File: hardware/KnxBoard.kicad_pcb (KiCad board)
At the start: 4 copper layers, 43 parts, among them J1 Conn_01x16, J2 Conn_01x16, J3 Conn_01x12, J4 Conn_01x02_Male, U0 STM32U575CIT6, U1 NCN5130, X1 FA-238

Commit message: Progress
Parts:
- C14, C19, C5_9, C6, JP0, JP1, R3: moved to B.Cu
- C16, C17: moved to F.Cu
- moved C12 47.0 mm to (113.3, 55.4), turned to 90 degrees
- moved R1 46.6 mm to (103.1, 53.3), turned to 180 degrees
- moved C16 44.5 mm to (98.6, 57.9), turned to 0 degrees
- moved C6 40.8 mm to (109.2, 57.4), turned to -90 degrees
- moved C14 37.9 mm to (102.1, 54.4), turned to 180 degrees
- moved R3 37.4 mm to (104.1, 65.0), turned to 180 degrees
- moved C17 37.4 mm to (95.5, 54.4), turned to 90 degrees
- moved C13 35.1 mm to (100.6, 62.5), turned to -90 degrees
- moved C10 33.5 mm to (98.6, 59.9)
- moved C20 32.1 mm to (115.8, 62.0), turned to 90 degrees
- moved R5 32.0 mm to (110.2, 65.0)
- moved R2 29.3 mm to (94.5, 67.1), turned to 180 degrees
- moved C15 28.8 mm to (113.3, 62.0), turned to -90 degrees
- moved R4 24.6 mm to (104.1, 65.0)
- moved C19 23.8 mm to (93.0, 71.1), turned to 90 degrees
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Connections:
- C6 pad 2: GND -> GNDREF
- JP2 pad 2: /MCU/PH1 -> KNX_RESETB
- U1 pad 23: GND -> GNDREF
- U1 pad 24: GND -> GNDREF
- U1 pad 25: GND -> GNDREF
- U1 pad 26: GND -> GNDREF
- U1 pad 29: GND -> GNDREF
- U1 pad 31: GND -> GNDREF
- U1 pad 33: GND -> GNDREF
- U1 pad 41: GND -> GNDREF
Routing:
- net GNDREF: track 100.1 -> 232.5 mm, vias 5 -> 13
- net KNX_RESETB: track 0.00 -> 72.0 mm, vias 0 -> 1
- net KNX_RXD: track 1.60 -> 62.7 mm, vias 1 -> 3
- net KNX_TXD: track 0.00 -> 55.9 mm, vias 0 -> 3
- net VDD: track 115.2 -> 166.7 mm, vias 7 -> 6
- net +3V3: track 0.00 -> 43.5 mm, vias 0 -> 3
- net Net-(C14-Pad2): track 0.00 -> 40.4 mm, vias 0 -> 2
- net KNX_SAVEB: track 0.00 -> 39.2 mm, vias 0 -> 2
- net +12V: track 0.00 -> 29.6 mm, vias 0 -> 1
- net Net-(R6-Pad1): track 0.00 -> 26.8 mm, vias 0 -> 2
- net /KNXIFACE/Vfilt: track 0.00 -> 23.9 mm, vias 0 -> 3
- net Net-(C17-Pad2): track 0.00 -> 20.6 mm, vias 0 -> 2
- net Led: track 32.8 -> 16.5 mm
- net Net-(L1-Pad1): track 0.00 -> 15.8 mm, vias 0 -> 2
- net /MCU/DEBUG_JTMS-SWDIO: track 27.3 -> 11.9 mm, vias 1 -> 0
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- added copper zone on B.Cu, net GNDREF
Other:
- board outline added: 41.8 x 41.9 mm

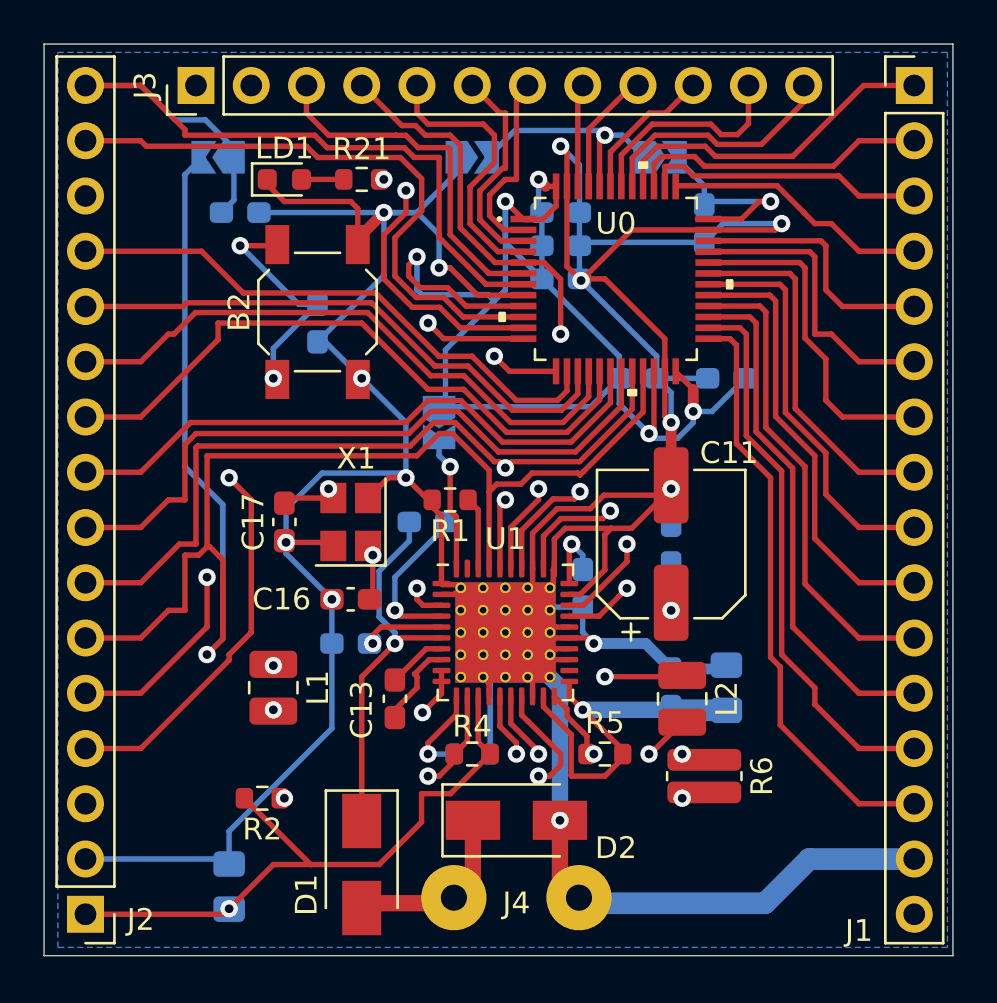
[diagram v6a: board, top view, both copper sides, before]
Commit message: Switch to STM32G491KEU6 with NCN5130
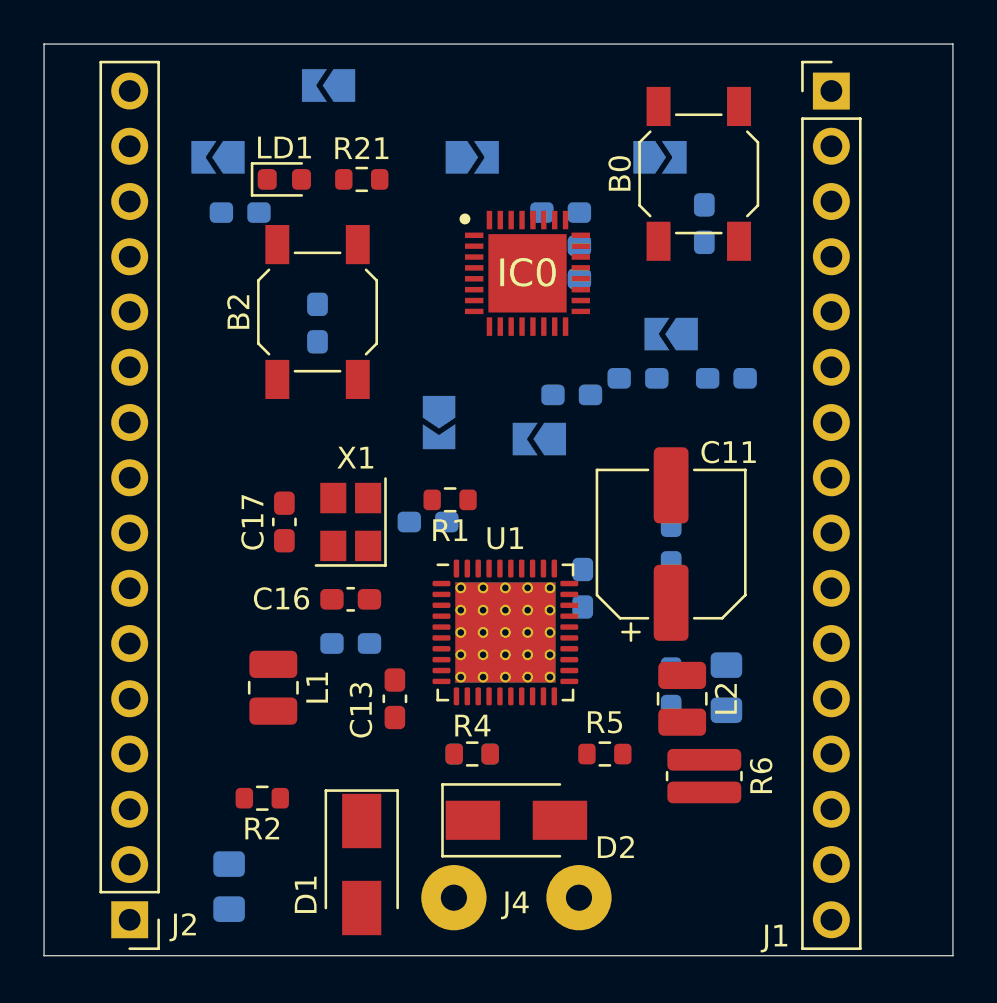
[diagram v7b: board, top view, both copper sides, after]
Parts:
- removed J3: Conn_01x12, Connector_PinHeader_2.54mm:PinHeader_1x12_P2.54mm_Vertical
- removed U0: STM32U575CIT6, KnxBoard:STM32U575CIT6
- added B0: RESET, Button_Switch_SMD:SW_SPST_SKQG_WithStem, F.Cu at (114.6, 38.4)
- added C1: 100 nF, Capacitor_SMD:C_0603_1608Metric_Pad1.08x0.95mm_HandSolder, B.Cu at (108.7, 48.5)
- added IC0: STM32G491KEU6, KnxBoard:STM32G491KEU6, F.Cu at (106.7, 42.9)
- added JP4: Bootflash, Jumper:SolderJumper-2_P1.3mm_Open_TrianglePad1.0x1.5mm, B.Cu at (97.5, 34.3)
- added JP5: Bootloader, Jumper:SolderJumper-2_P1.3mm_Open_TrianglePad1.0x1.5mm, B.Cu at (113.3, 45.7)
- added JP6: RESETB_NRST, Jumper:SolderJumper-2_P1.3mm_Open_TrianglePad1.0x1.5mm, B.Cu at (107.2, 50.5)
- moved J1 3.82 mm to (120.7, 34.5)
- moved J2 2.05 mm to (88.4, 72.6)
- renumbered C3_48 to C3, C3_36 to C4, C3_25 to C5
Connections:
- C5 pad 1: VDD -> GNDREF
- C5 pad 2: GNDREF -> VDD
- J1 pad 1: /MCU/PB4 -> GNDREF
- J1 pad 10: /MCU/PA8 -> /MCU/DEBUG_JTCK-SWCLK
- J1 pad 11: /MCU/PB15 -> /MCU/DEBUG_JTMS-SWDIO
- J1 pad 12: /MCU/PB14 -> KNX_SAVEB
- J1 pad 13: /MCU/PB13 -> KNX_RESETB
- J1 pad 14: /MCU/PB12 -> KNX_RXD
- J1 pad 15: GNDREF -> KNX_TXD
- J1 pad 16: VDD -> Prog
- J1 pad 2: /MCU/DEBUG_JTDA-SWO -> VDD
- J1 pad 3: /MCU/DEBUG_JTDI -> /MCU/PB8
- J1 pad 4: /MCU/DEBUG_JTCK-SWCLK -> /MCU/PB7
- J1 pad 5: /MCU/DEBUG_JTMS-SWDIO -> /MCU/PB6
- J1 pad 6: /MCU/PA12 -> /MCU/PB5
- J1 pad 7: /MCU/PA11 -> /MCU/PB4
- J1 pad 8: /MCU/DEBUG_UART_RX -> /MCU/DEBUG_JTDA-SWO
- J1 pad 9: /MCU/DEBUG_UART_TX -> /MCU/DEBUG_JTDI
- J2 pad 10: /MCU/PA7 -> /MCU/DEBUG_UART_RX
- J2 pad 11: /MCU/PA6 -> /MCU/DEBUG_UART_TX
- J2 pad 12: /MCU/PA5 -> /MCU/PA1
- J2 pad 13: /MCU/PA4 -> /MCU/PA0
- J2 pad 14: /MCU/PA1 -> NRST
- J2 pad 15: /MCU/PA0 -> /MCU/PF1
- J2 pad 16: NRST -> CLK16
- J2 pad 4: KNX_RXD -> GNDREF
- J2 pad 5: KNX_TXD -> Led
- J2 pad 6: KNX_RESETB -> /MCU/PA7
- J2 pad 7: KNX_SAVEB -> /MCU/PA6
- J2 pad 8: /MCU/PB1 -> /MCU/PA5
- J2 pad 9: /MCU/PB0 -> /MCU/PA4
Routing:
- net GNDREF: track 232.5 -> 0.00 mm, vias 13 -> 0
- net VDD: track 166.7 -> 0.00 mm, vias 6 -> 0
- net KNX_RESETB: track 72.0 -> 0.00 mm, vias 1 -> 0
- net KNX_RXD: track 62.7 -> 0.00 mm, vias 3 -> 0
- net KNX_TXD: track 55.9 -> 0.00 mm, vias 3 -> 0
- net +3V3: track 43.5 -> 0.00 mm, vias 3 -> 0
- net Prog: track 41.5 -> 0.00 mm, vias 2 -> 0
- net Net-(C14-Pad2): track 40.4 -> 0.00 mm, vias 2 -> 0
- net KNX_SAVEB: track 39.2 -> 0.00 mm, vias 2 -> 0
- net NRST: track 37.0 -> 0.00 mm
- net CLK16: track 31.7 -> 0.00 mm, vias 2 -> 0
- net /MCU/PB1: track 31.6 -> 0.00 mm
- net /MCU/PA7: track 29.9 -> 0.00 mm
- net +12V: track 29.6 -> 0.00 mm, vias 1 -> 0
- net /MCU/PB0: track 28.5 -> 0.00 mm
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- removed copper zone on B.Cu, net GNDREF

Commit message: Add 3D model and remove old parts
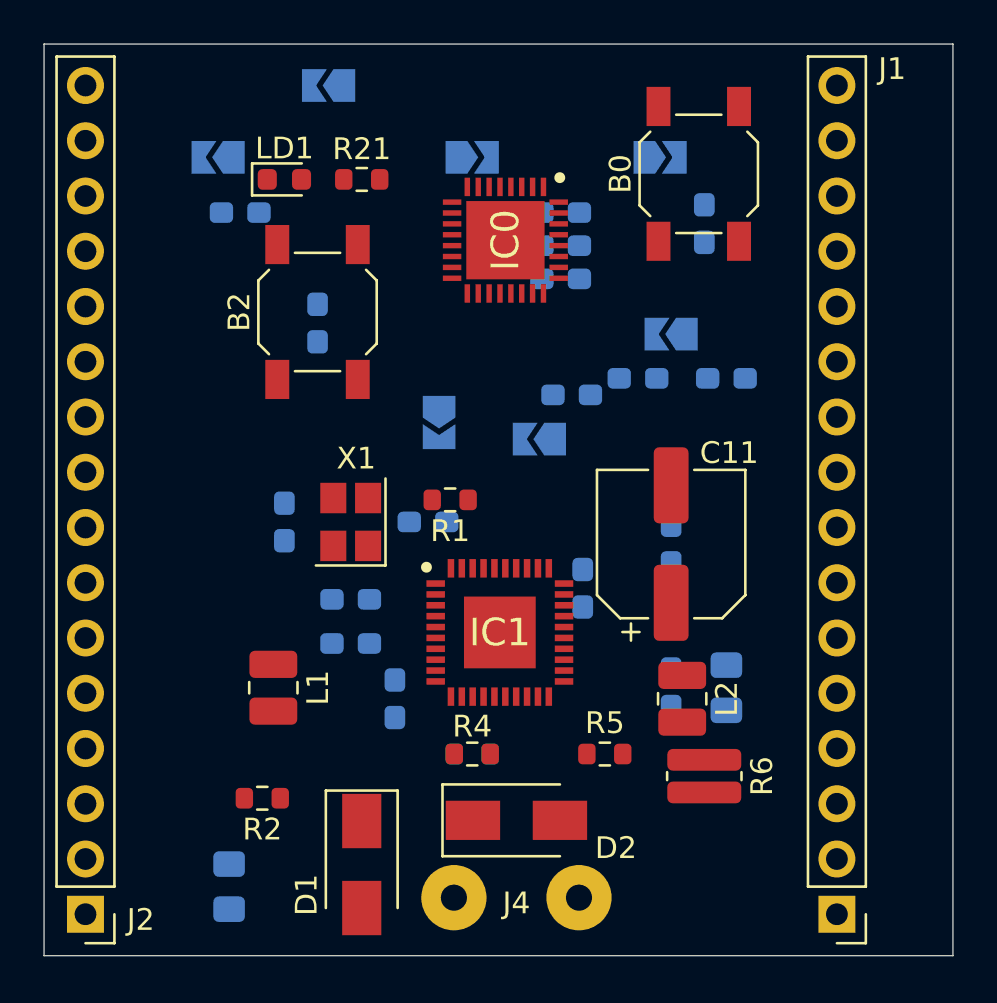
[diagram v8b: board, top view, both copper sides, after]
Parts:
- removed U1: NCN5130, Package_DFN_QFN:QFN-40-1EP_6x6mm_P0.5mm_EP4.6x4.6mm_ThermalVias
- added IC1: NCN5130, KnxBoard:NCN5130, F.Cu at (105.4, 59.4)
- C13, C16, C17: moved to B.Cu
- moved J1 37.8 mm to (120.9, 72.4), turned to 180 degrees
- moved J2 2.05 mm to (86.4, 72.4)
- moved IC0 1.83 mm to (105.7, 41.4), turned to -90 degrees
- turned C16 to 180 degrees
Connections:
- J1 pad 1: GNDREF -> Prog
- J1 pad 10: /MCU/DEBUG_JTCK-SWCLK -> /MCU/PB4
- J1 pad 11: /MCU/DEBUG_JTMS-SWDIO -> /MCU/PB5
- J1 pad 12: KNX_SAVEB -> /MCU/PB6
- J1 pad 13: KNX_RESETB -> /MCU/PB7
- J1 pad 14: KNX_RXD -> /MCU/PB8
- J1 pad 15: KNX_TXD -> VDD
- J1 pad 16: Prog -> GNDREF
- J1 pad 2: VDD -> KNX_TXD
- J1 pad 3: /MCU/PB8 -> KNX_RXD
- J1 pad 4: /MCU/PB7 -> KNX_RESETB
- J1 pad 5: /MCU/PB6 -> KNX_SAVEB
- J1 pad 6: /MCU/PB5 -> /MCU/DEBUG_JTMS-SWDIO
- J1 pad 7: /MCU/PB4 -> /MCU/DEBUG_JTCK-SWCLK
- J1 pad 8: /MCU/DEBUG_JTDA-SWO -> /MCU/DEBUG_JTDI
- J1 pad 9: /MCU/DEBUG_JTDI -> /MCU/DEBUG_JTDA-SWO
